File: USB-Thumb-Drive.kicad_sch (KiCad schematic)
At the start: 0 parts

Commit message: Création des feuilles de chaque blocs et hiérarchie globale
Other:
- added sheet BUCK_CONVERTER (buck_converter.kicad_sch)
- added sheet ORING_POWER (oring_power.kicad_sch)
- added sheet RP2040 (rp2040.kicad_sch)
- added sheet USB_BRIDGE (usb_bridge.kicad_sch)
- added sheet eMMC_STORAGE (emmc_storage.kicad_sch)
- company: (none) -> Guillaume LOUIS
- title: (none) -> USB Smart Drive
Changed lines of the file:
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@@
 	(generator_version "10.0")
 	(paper "A4")
+	(title_block
+		(title "USB Smart Drive")
+		(date "2026-06-05")
+		(rev "Revision 1.0")
+		(company "Guillaume LOUIS")
+		(comment 1 "Root and organisation ")
+	)
+	(sheet
+		(at 143.51 93.98)
+		(size 15.24 15.24)
+		(exclude_from_sim no)
+		(in_bom yes)
+		(on_board yes)
+		(dnp no)
+		(fields_autoplaced yes)
+		(stroke
+			(width 0.1524)
+			(type solid)
+		)
+		(fill
+			(color 0 0 0 0)
+		)
+		(property "Sheetname" "BUCK_CONVERTER"
+			(at 143.51 93.2684 0)
+			(show_name no)
+			(do_not_autoplace no)
+			(effects
+				(font
+					(size 1.27 1.27)
+				)
+				(justify left bottom)
+			)
+		)
+		(property "Sheetfile" "buck_converter.kicad_sch"
+			(at 143.51 109.8046 0)
+			(show_name no)
+			(do_not_autoplace no)
+			(effects
+				(font
+					(size 1.27 1.27)
+				)
+				(justify left top)
+			)
+		)
+		(instances
+			(project "USB-Thumb-Drive"
+				(path "/61284d1f-c8a6-45b4-aa7f-ae2816ab8ea5"
+					(page "3")
+				)
+			)
+		)
+	)
+	(sheet
+		(at 184.15 110.49)
+		(size 22.86 26.67)
+		(exclude_from_sim no)
+		(in_bom yes)
+		(on_board yes)
+		(dnp no)
+		(fields_autoplaced yes)
+		(stroke
+			(width 0.1524)
+			(type solid)
+		)
+		(fill
+			(color 0 0 0 0)
+		)
+		(property "Sheetname" "RP2040"
+			(at 184.15 109.7784 0)
+			(show_name no)
+			(do_not_autoplace no)
+			(effects
+				(font
+					(size 1.27 1.27)
+				)
+				(justify left bottom)
+			)
+		)
+		(property "Sheetfile" "rp2040.kicad_sch"
+			(at 184.15 137.7446 0)
+			(show_name no)
+			(do_not_autoplace no)
+			(effects
+				(font
+					(size 1.27 1.27)
+				)
+				(justify left top)
+			)
+		)
+		(instances
+			(project "USB-Thumb-Drive"
+				(path "/61284d1f-c8a6-45b4-aa7f-ae2816ab8ea5"
+					(page "5")
+				)
+			)
+		)
+	)
+	(sheet
+		(at 95.25 52.07)
+		(size 27.94 29.21)
+		(exclude_from_sim no)
+		(in_bom yes)
+		(on_board yes)
+		(dnp no)
+		(fields_autoplaced yes)
+		(stroke
+			(width 0.1524)
+			(type solid)
+		)
+		(fill
+			(color 0 0 0 0)
+		)
+		(property "Sheetname" "USB_BRIDGE"
+			(at 95.25 51.3584 0)
+			(show_name no)
+			(do_not_autoplace no)
+			(effects
+				(font
+					(size 1.27 1.27)
+				)
+				(justify left bottom)
+			)
+		)
+		(property "Sheetfile" "usb_bridge.kicad_sch"
+			(at 95.25 81.8646 0)
+			(show_name no)
+			(do_not_autoplace no)
+			(effects
+				(font
+					(size 1.27 1.27)
+				)
+				(justify left top)
+			)
+		)
+		(instances
+			(project "USB-Thumb-Drive"
+				(path "/61284d1f-c8a6-45b4-aa7f-ae2816ab8ea5"
+					(page "4")
+				)
+			)
+		)
+	)
+	(sheet
+		(at 101.6 97.79)
+		(size 25.4 21.59)
+		(exclude_from_sim no)
+		(in_bom yes)
+		(on_board yes)
+		(dnp no)
+		(fields_autoplaced yes)
+		(stroke
+			(width 0.1524)
+			(type solid)
+		)
+		(fill
+			(color 0 0 0 0)
+		)
+		(property "Sheetname" "ORING_POWER"
+			(at 101.6 97.0784 0)
+			(show_name no)
+			(do_not_autoplace no)
+			(effects
+				(font
+					(size 1.27 1.27)
+				)
+				(justify left bottom)
+			)
+		)
+		(property "Sheetfile" "oring_power.kicad_sch"
+			(at 101.6 119.9646 0)
+			(show_name no)
+			(do_not_autoplace no)
+			(effects
+				(font
+					(size 1.27 1.27)
+				)
+				(justify left top)
+			)
+		)
+		(instances
+			(project "USB-Thumb-Drive"
+				(path "/61284d1f-c8a6-45b4-aa7f-ae2816ab8ea5"
+					(page "2")
+				)
+			)
+		)
+	)
+	(sheet
+		(at 140.97 54.61)
+		(size 26.67 24.13)
+		(exclude_from_sim no)
+		(in_bom yes)
+		(on_board yes)
+		(dnp no)
+		(fields_autoplaced yes)
+		(stroke
+			(width 0.1524)
+			(type solid)
+		)
+		(fill
+			(color 0 0 0 0)
+		)
+		(property "Sheetname" "eMMC_STORAGE"
+			(at 140.97 53.8984 0)
+			(show_name no)
+			(do_not_autoplace no)
+			(effects
+				(font
+					(size 1.27 1.27)
+				)
+				(justify left bottom)
+			)
+		)
+		(property "Sheetfile" "emmc_storage.kicad_sch"
+			(at 140.97 79.3246 0)
+			(show_name no)
+			(do_not_autoplace no)
+			(effects
+				(font
+					(size 1.27 1.27)
+				)
+				(justify left top)
+			)
+		)
+		(instances
+			(project "USB-Thumb-Drive"
+				(path "/61284d1f-c8a6-45b4-aa7f-ae2816ab8ea5"
+					(page "6")
+				)
+			)
+		)
+	)
 	(sheet_instances
 		(path "/"

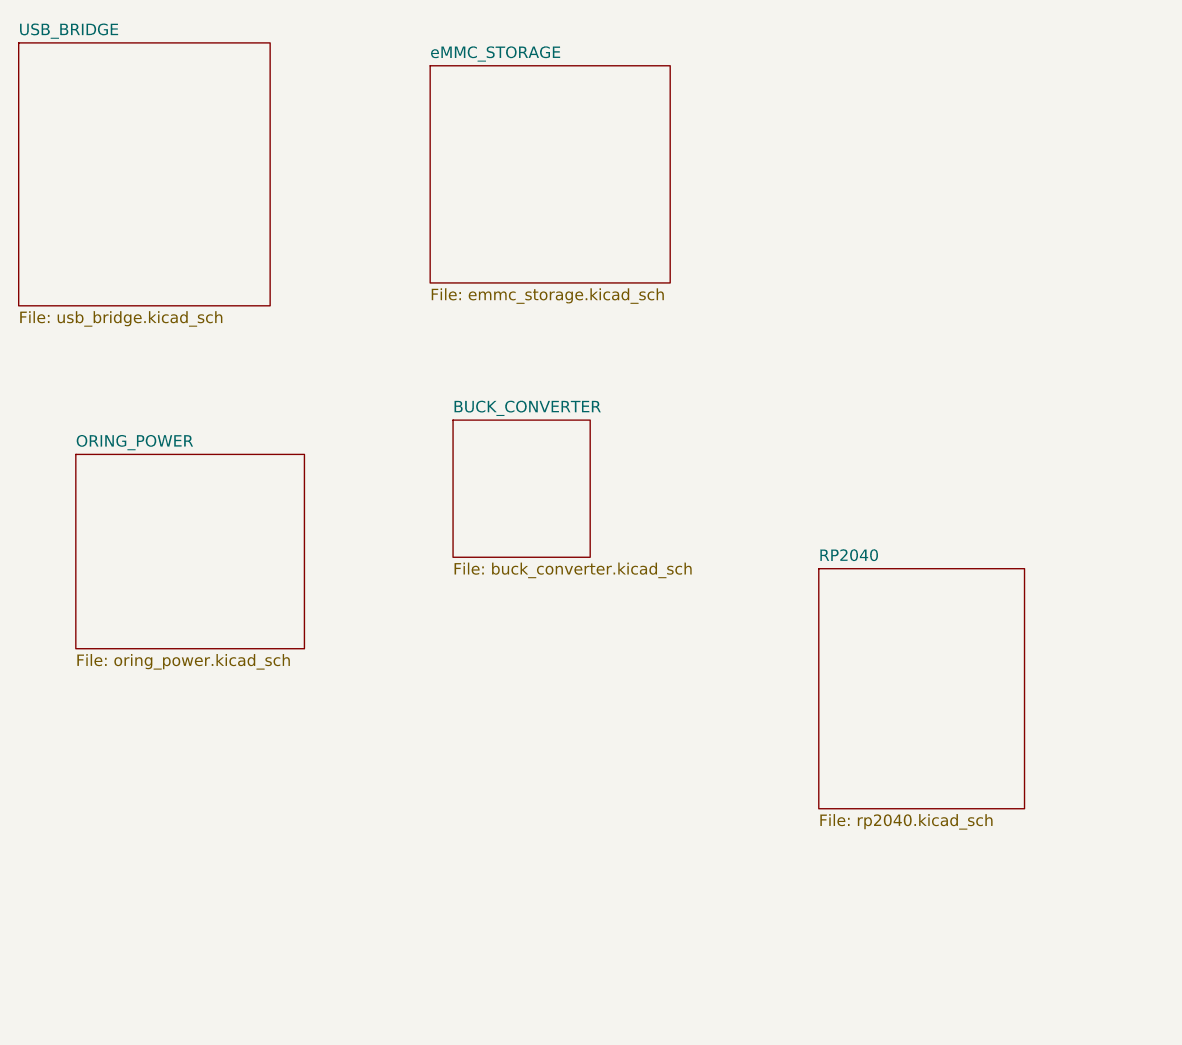
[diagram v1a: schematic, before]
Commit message: Buck converter sheet done
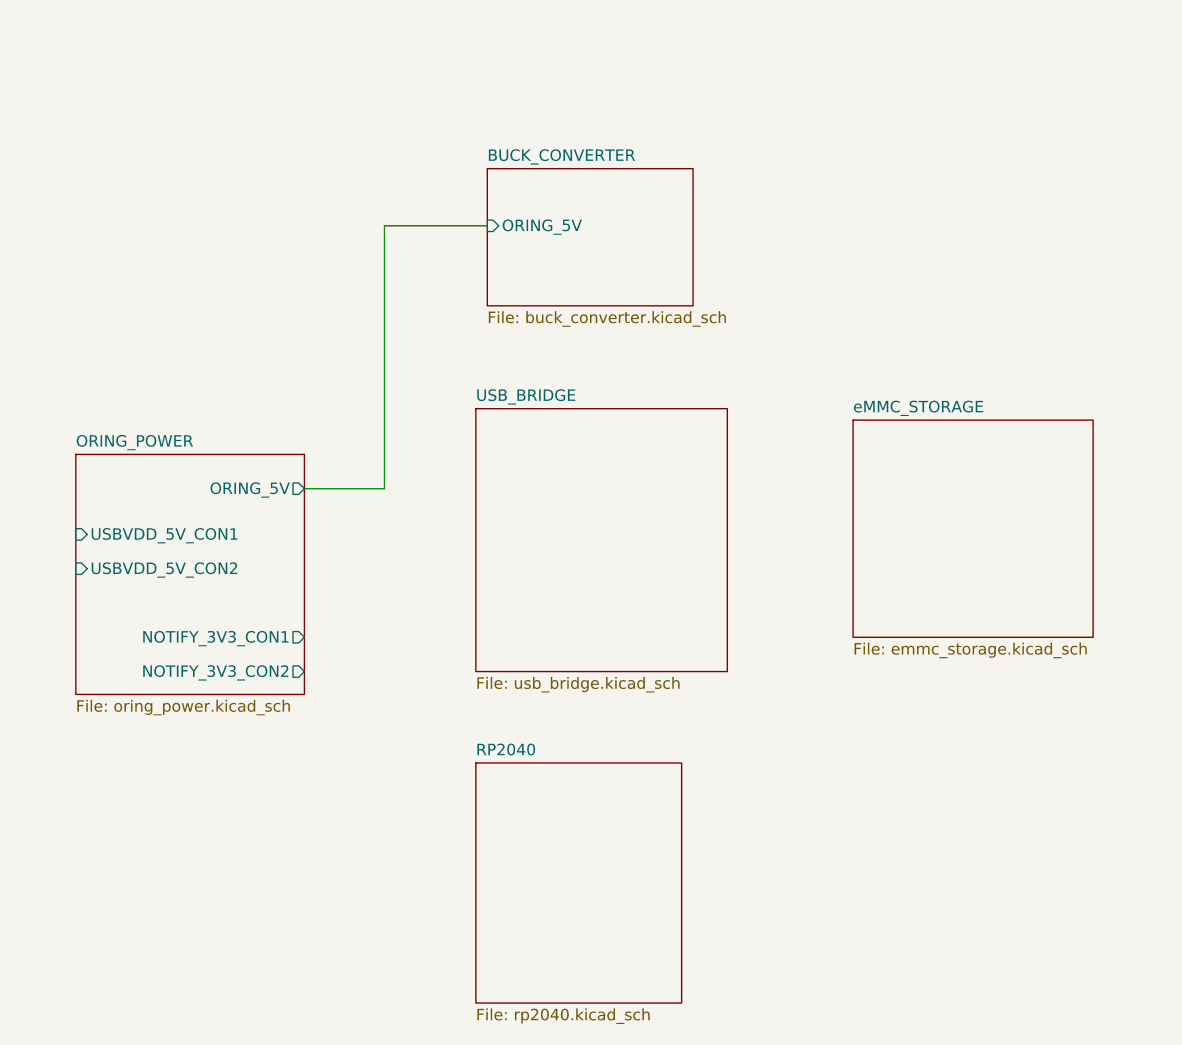
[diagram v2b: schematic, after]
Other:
- sheet BUCK_CONVERTER ports: added ORING_5V; removed none
- sheet ORING_POWER ports: added NOTIFY_3V3_CON1, NOTIFY_3V3_CON2, ORING_5V, USBVDD_5V_CON1, USBVDD_5V_CON2; removed none

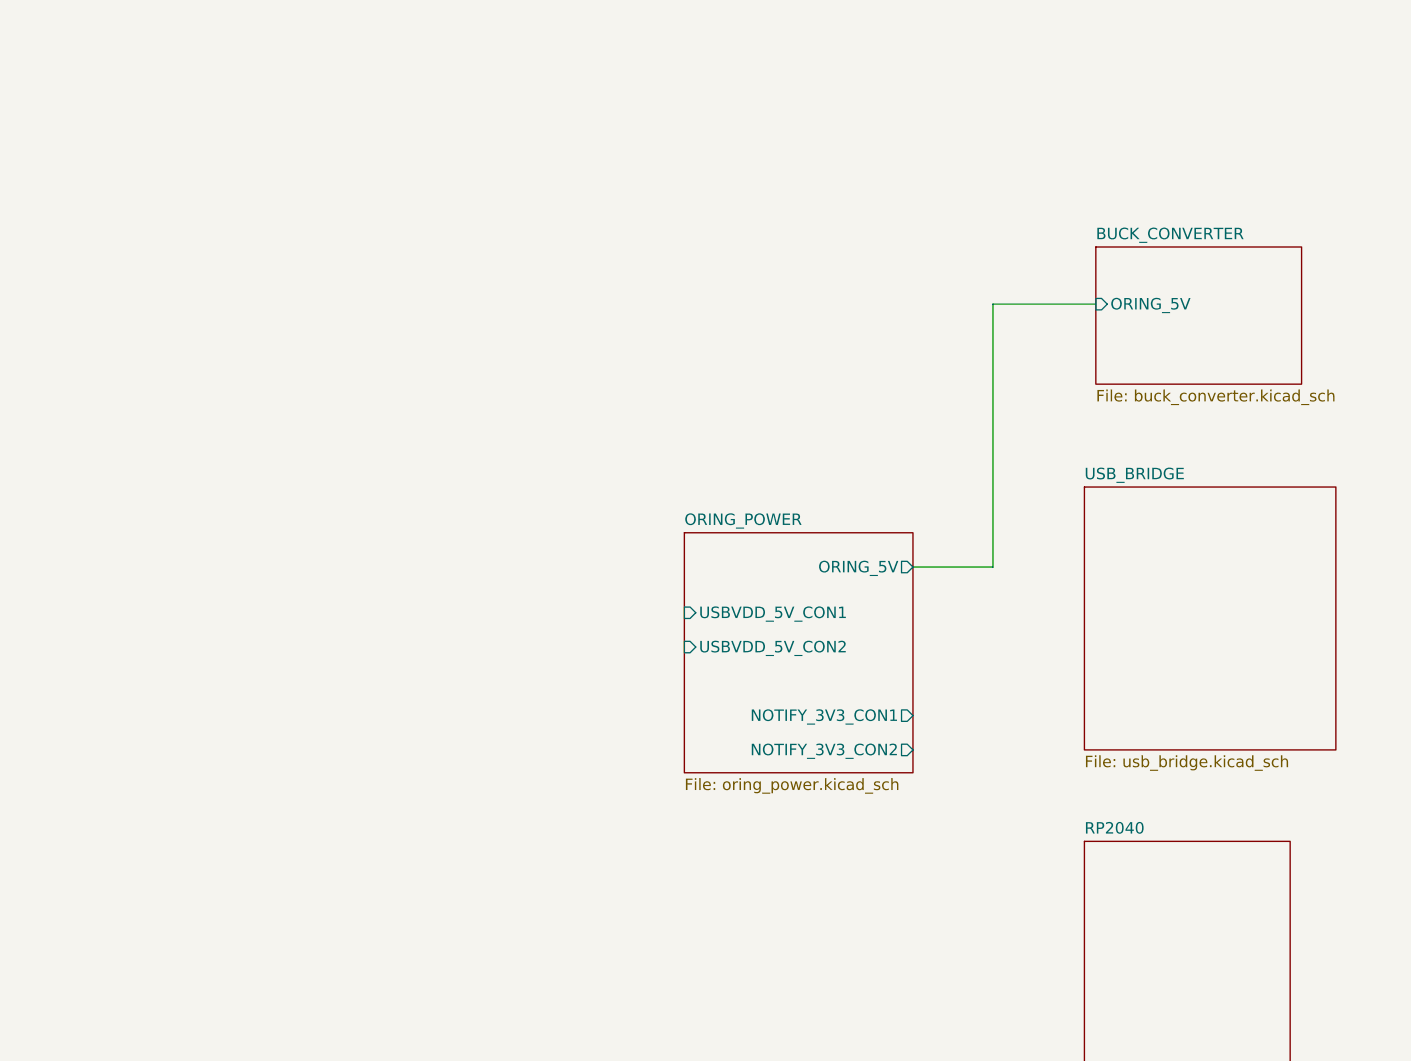
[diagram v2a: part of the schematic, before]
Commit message: progress USB parts of the schematic
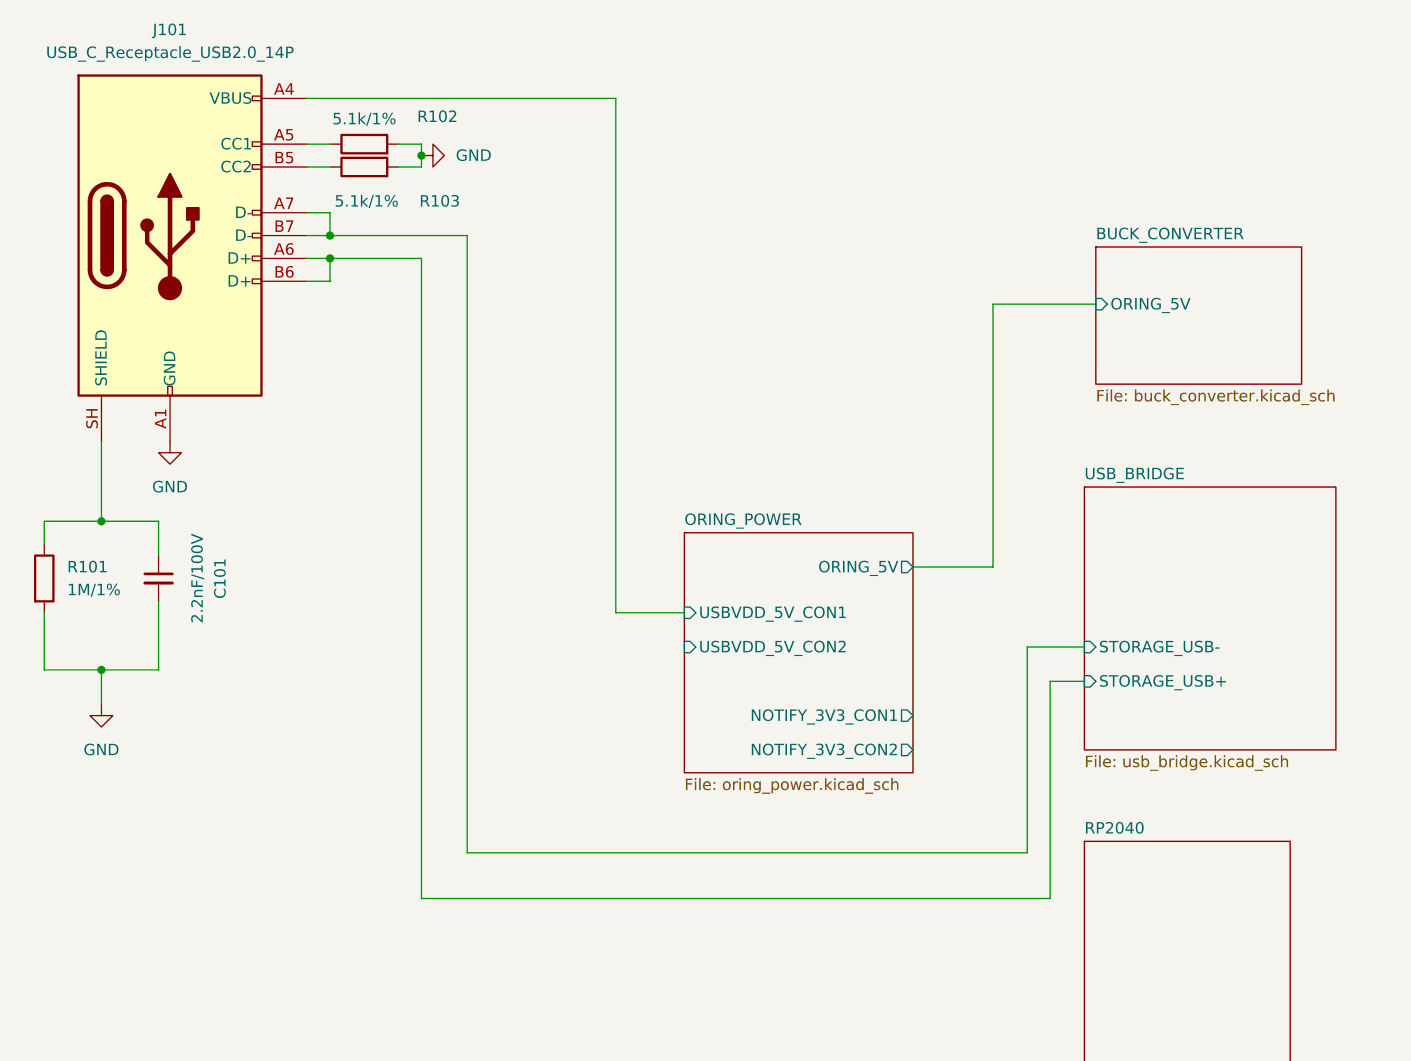
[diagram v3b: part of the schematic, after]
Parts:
- added C101: 2.2nF/100V, SparkFun-Capacitor:C_0603_1608Metric, symbol SparkFun-Capacitor:C_Small
- added J101: USB_C_Receptacle_USB2.0_14P, Connector_USB:USB_C_Receptacle_XKB_U262-16XN-4BVC11, symbol Connector:USB_C_Receptacle_USB2.0_14P
- added R101: 1M/1%, Resistor_SMD:R_01005_0402Metric, symbol Device:R
- added R102, R103: 5.1k/1%, Resistor_SMD:R_01005_0402Metric, symbol Device:R
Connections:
- net ORING_POWER/USBVDD_5V_CON1: now also J101.A4 (VBUS), J101.A9 (VBUS), J101.B4 (VBUS), J101.B9 (VBUS)
- new net: J101.A5 (CC1), R102.1
- new net: J101.B5 (CC2), R103.1
- new net: C101.1, J101.SH (SHIELD), R101.1
- new net GND: C101.2, J101.A1 (GND), J101.A12 (GND), J101.B1 (GND), J101.B12 (GND), R101.2, R102.2, R103.2
- new net USB_BRIDGE/STORAGE_USB+: J101.A6 (D+), J101.B6 (D+)
- new net USB_BRIDGE/STORAGE_USB-: J101.A7 (D-), J101.B7 (D-)
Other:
- sheet USB_BRIDGE ports: added STORAGE_USB+, STORAGE_USB-; removed none
